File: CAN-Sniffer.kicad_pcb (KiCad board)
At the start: 2 copper layers, 70 x 50 mm, 29 parts, among them J1 CANConnIn, J2 CANConnOut, U1 Nucleo_L432KC, U2 ADM3055E, U3 CDSOT23-T24CAN

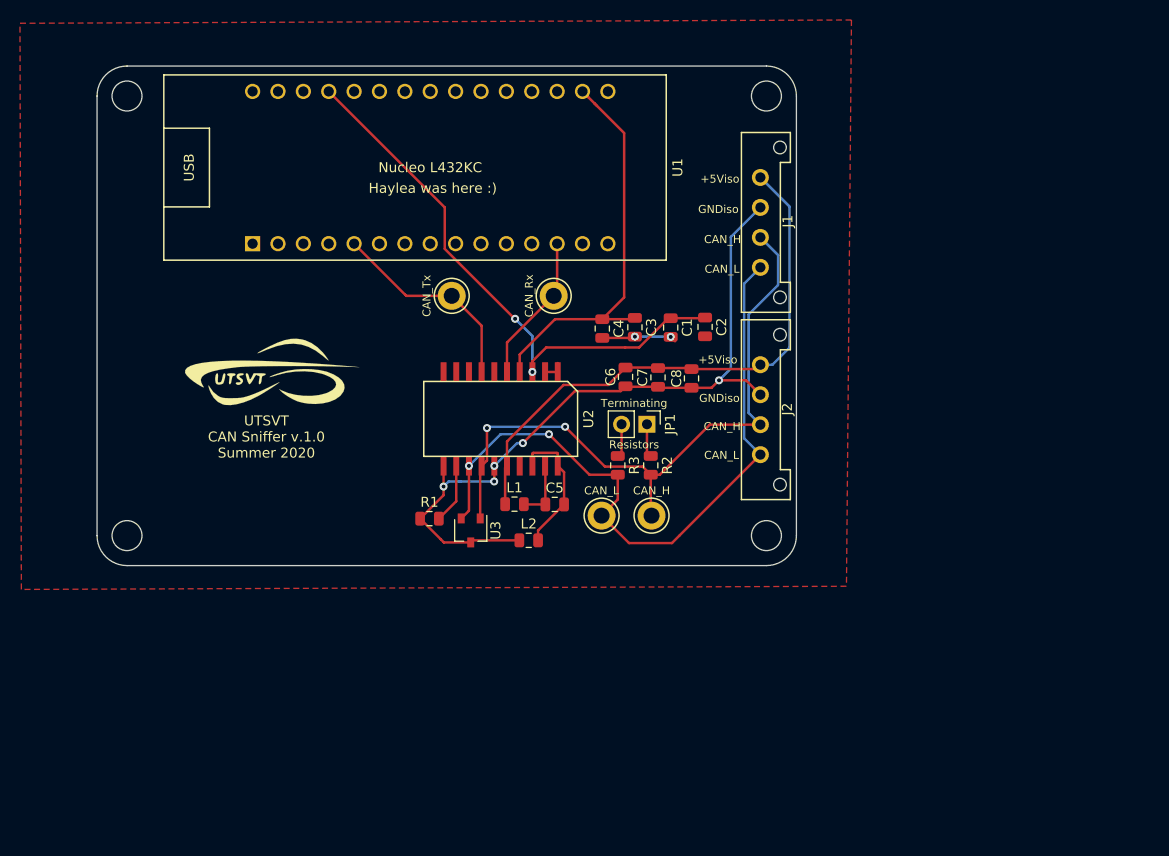
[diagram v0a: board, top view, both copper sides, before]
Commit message: Rearranged PCB Layout for CAN Sniffer
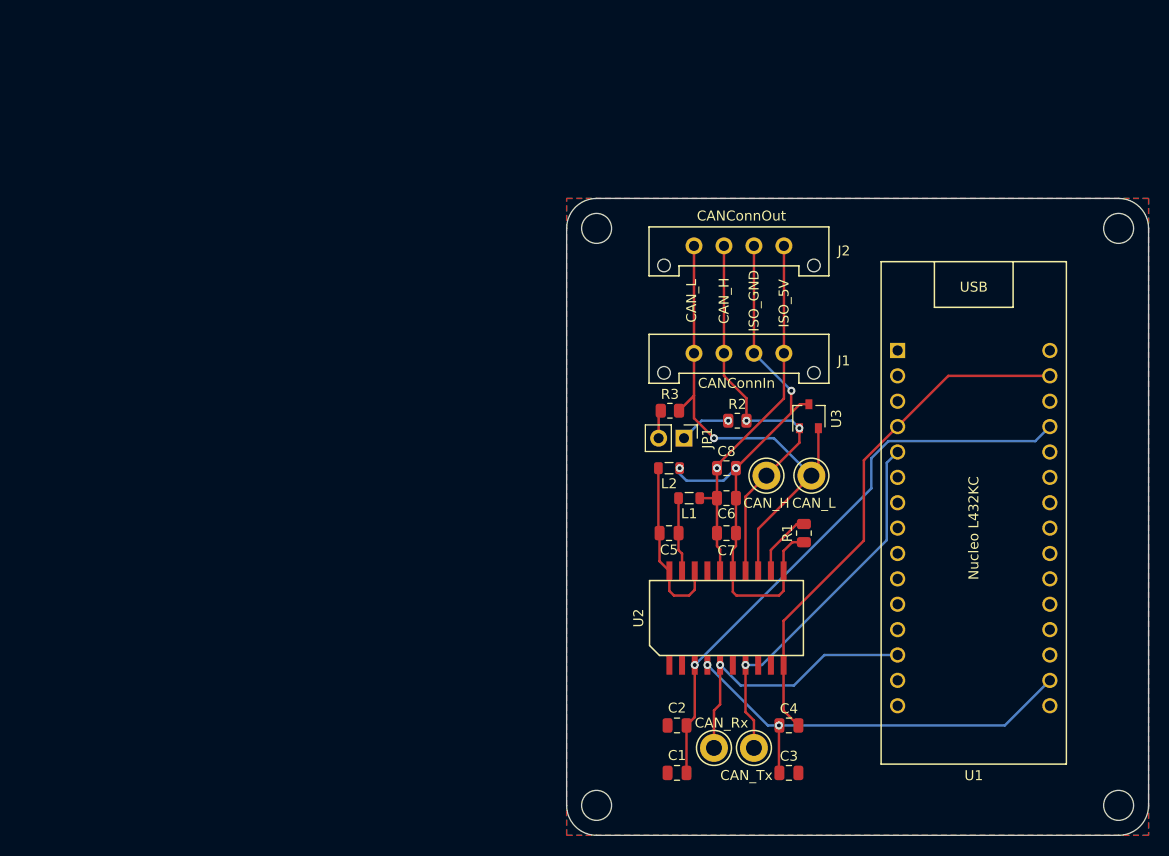
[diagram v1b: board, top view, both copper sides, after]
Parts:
- added G***: LOGO, hinata:HinataFP, B.Cu at (175.8, 132.0)
- LOGO1: moved to B.Cu
- moved LOGO2 67.8 mm to (186.5, 109.5)
- moved U1 65.3 mm to (187.8, 109.8), turned to 270 degrees
- moved TP1 54.4 mm to (165.8, 131.8), turned to 270 degrees
- moved H3 54.2 mm to (150.0, 137.5)
- moved LOGO1 52.1 mm to (163.2, 118.8), turned to 180 degrees
- moved H1 48.8 mm to (150.0, 79.8)
- moved TP2 48.0 mm to (161.8, 131.8), turned to 270 degrees
- moved C3 47.2 mm to (169.2, 134.2), turned to 0 degrees
- moved C1 44.6 mm to (158.1, 134.2), turned to 180 degrees
- moved H4 44.4 mm to (202.2, 137.5)
- moved C4 43.9 mm to (169.2, 129.5), turned to 0 degrees
- moved C2 40.0 mm to (158.1, 129.5), turned to 180 degrees
- moved H2 37.7 mm to (202.2, 79.8)
- moved R1 37.5 mm to (170.8, 110.2), turned to 90 degrees
- moved U3 35.7 mm to (171.2, 98.5), turned to 90 degrees
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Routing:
- net GND: track 9.77 -> 52.6 mm, vias 2 -> 0
- net /CAN_H: track 66.1 -> 40.6 mm
- net Net-(C6-Pad1): track 57.7 -> 37.2 mm, vias 0 -> 1
- net /CAN_L: track 69.0 -> 51.5 mm, vias 2 -> 1
- net /CAN_Tx: track 20.8 -> 37.2 mm, vias 0 -> 1
- net Net-(C6-Pad2): track 74.6 -> 59.7 mm, vias 5 -> 4
- net /CAN_Rx: track 14.9 -> 28.4 mm, vias 0 -> 1
- net Net-(C5-Pad2): track 13.8 -> 17.6 mm
- net +3V3: track 41.4 -> 43.5 mm, vias 0 -> 2
- net Net-(JP1-Pad1): track 3.34 -> 5.15 mm, vias 0 -> 1
- net +5V: track 56.9 -> 58.3 mm, vias 2 -> 1
- net Net-(C5-Pad1): track 6.03 -> 7.45 mm
- added copper zone on B.Cu, net GND
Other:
- board size 70 x 50 mm -> 58.2 x 63.8 mm
- board text added: "CANConnIn"
- board text added: "CANConnOut"
- board text added: "ISO_5V"
- board text added: "ISO_GND"
- board text added: "Renee :]"
- board text removed: "+5Viso"
- board text removed: "Dr. Gary Hallock"
- board text removed: "GNDiso"
- board text removed: "Haylea was here :)"
- board text removed: "Resistors"
- board text removed: "Terminating"
- board text removed: "UTSVT CAN Sniffer v.1.0 Summer 2020"
